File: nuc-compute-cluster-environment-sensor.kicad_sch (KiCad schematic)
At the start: 116 parts, among them J17 USB-C_GCT_USB4145-03-0070-C, J18 JST_SH_1x4_SM04B-SRSS-TB-LF-SN, U27 FT4232H_VQFN, U28 AP7370-33SA-7, U29 STM32G474CET6, U30 MB85RC1MTPNF-G, U31 SHT45, U32 BME280, Y2 Resonator_12MHz_ABM3B, Y3 Resonator_32.768kHz_ABS06, Y4 Resonator_8MHz_ABM3B

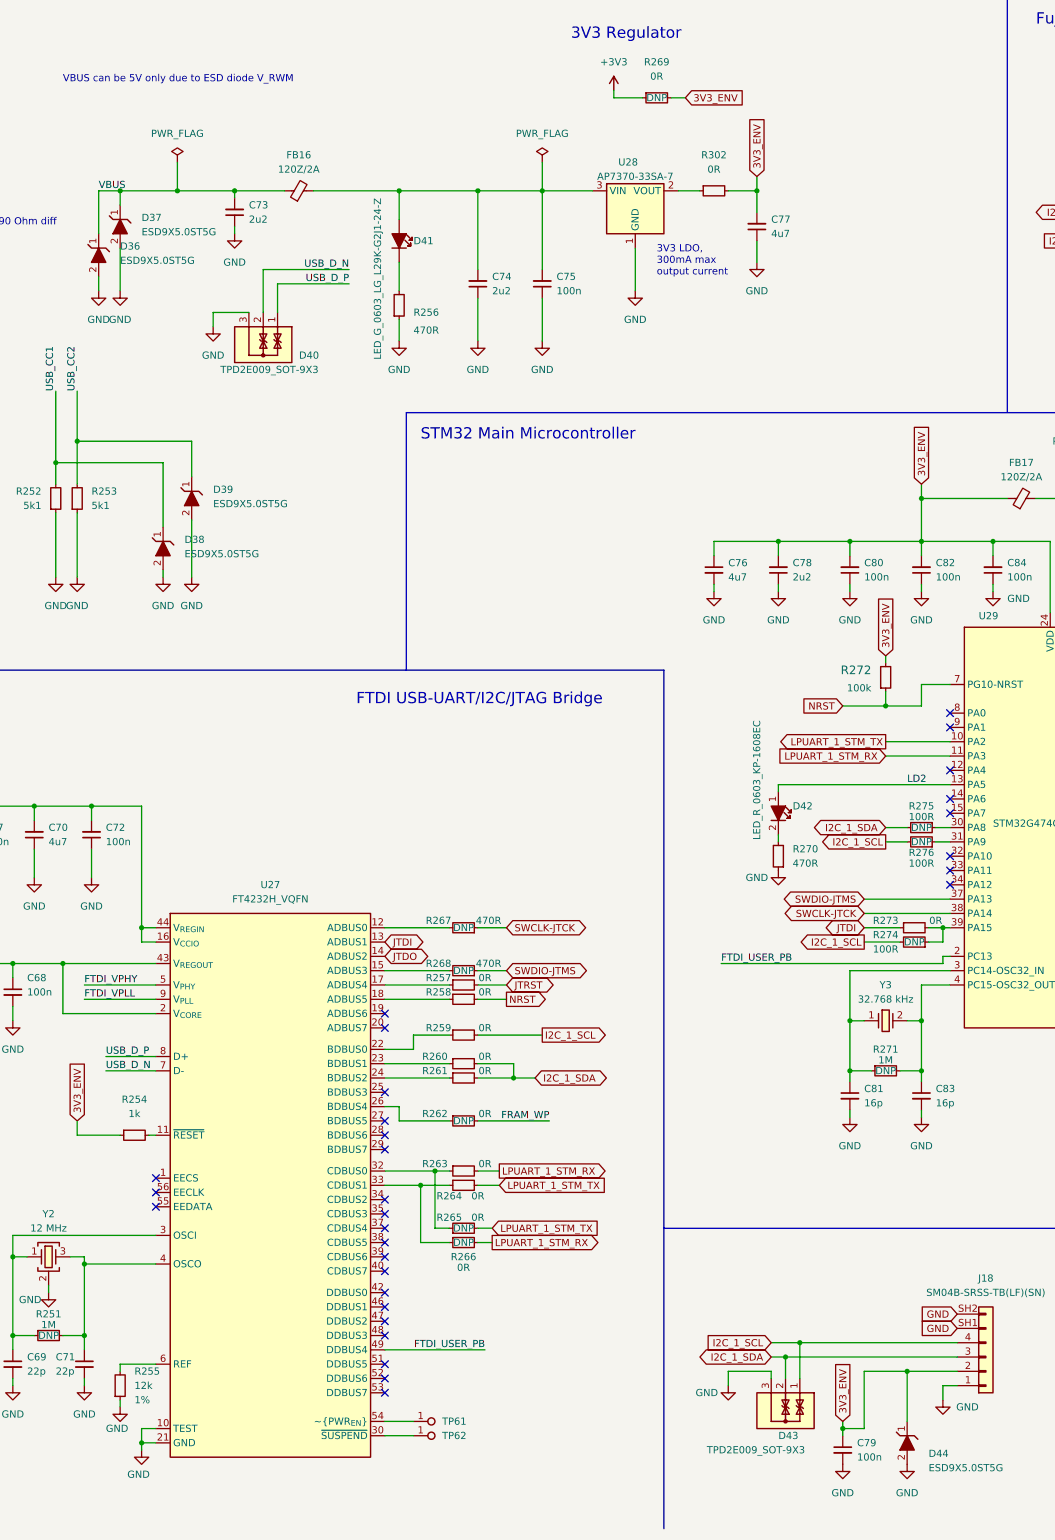
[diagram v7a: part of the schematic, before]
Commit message: Fix ESD diode symbol and GPU connector symbol
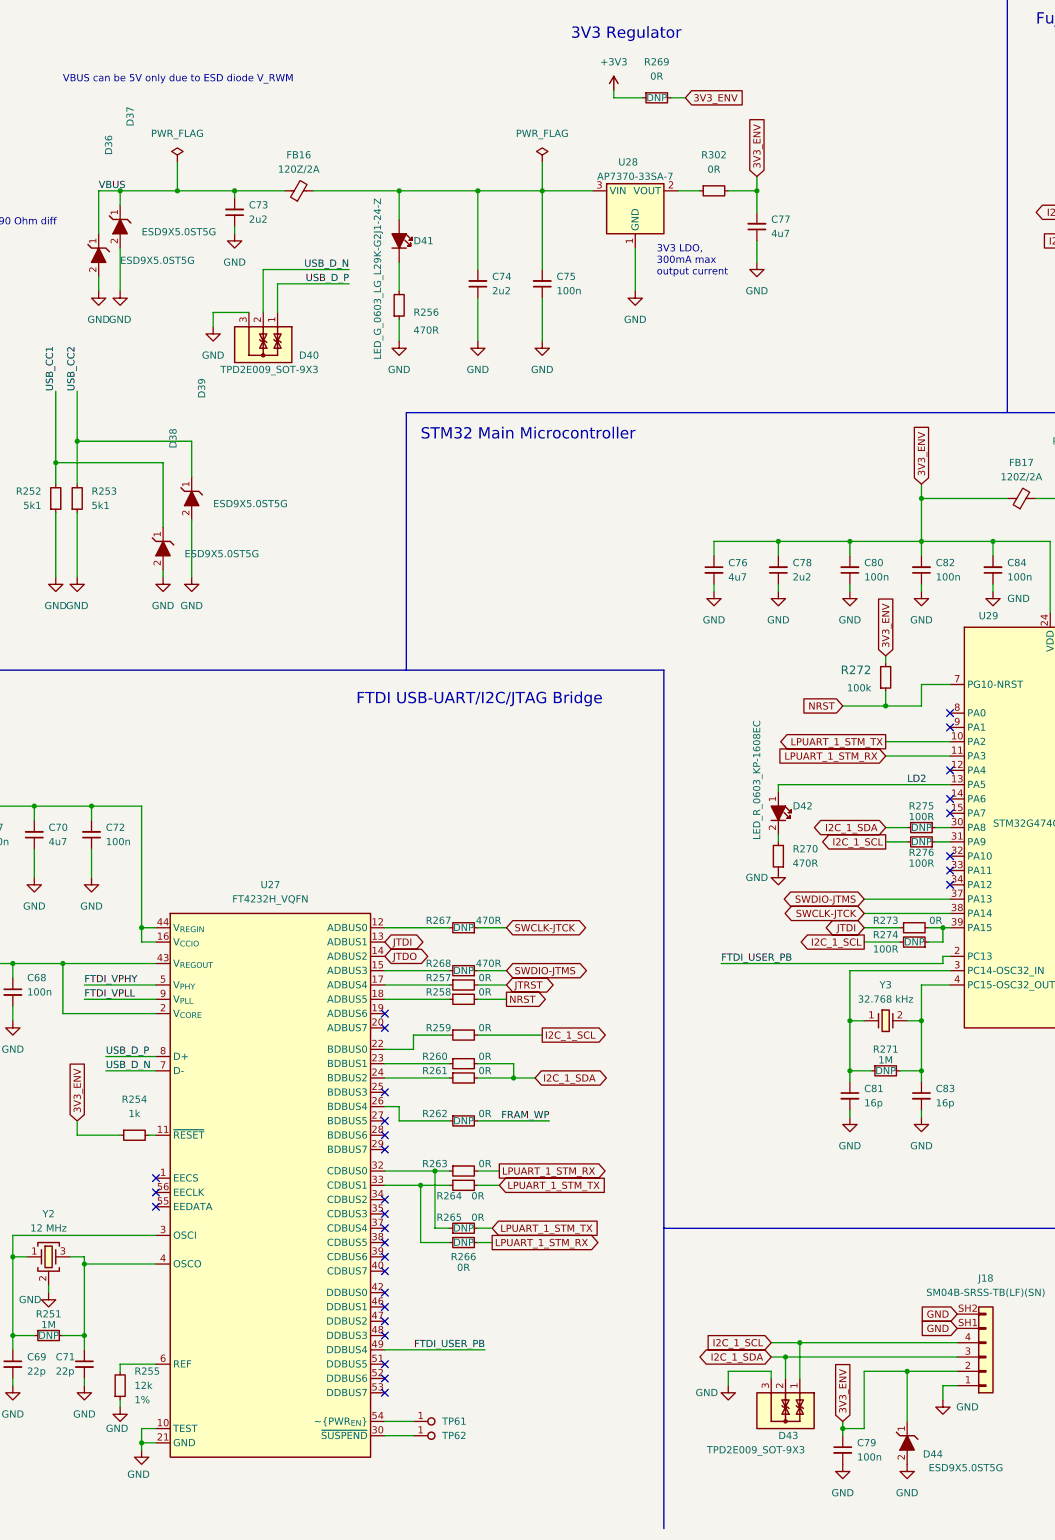
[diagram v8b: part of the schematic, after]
